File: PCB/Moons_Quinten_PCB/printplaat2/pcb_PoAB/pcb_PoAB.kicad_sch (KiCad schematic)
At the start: 34 parts, among them U9 ARDUINO_MKR_WAN_1310

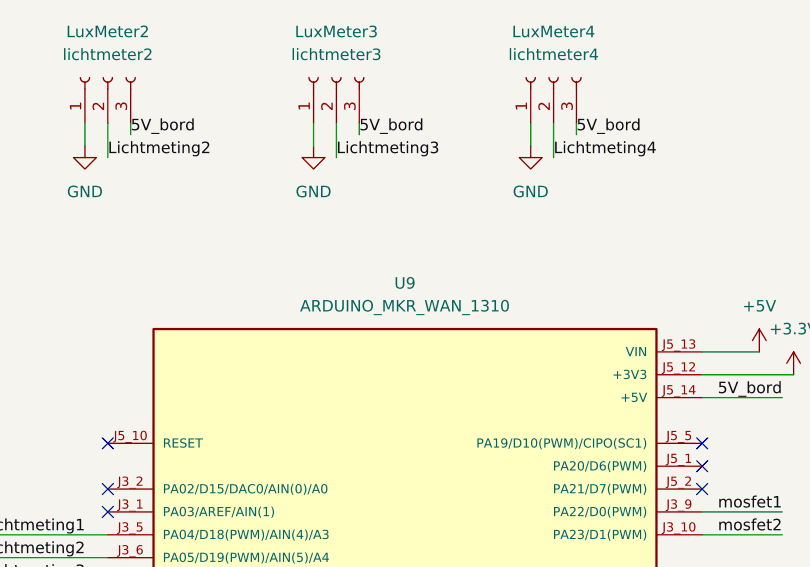
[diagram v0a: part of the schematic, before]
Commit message: pcb baseplate en docs aangepast
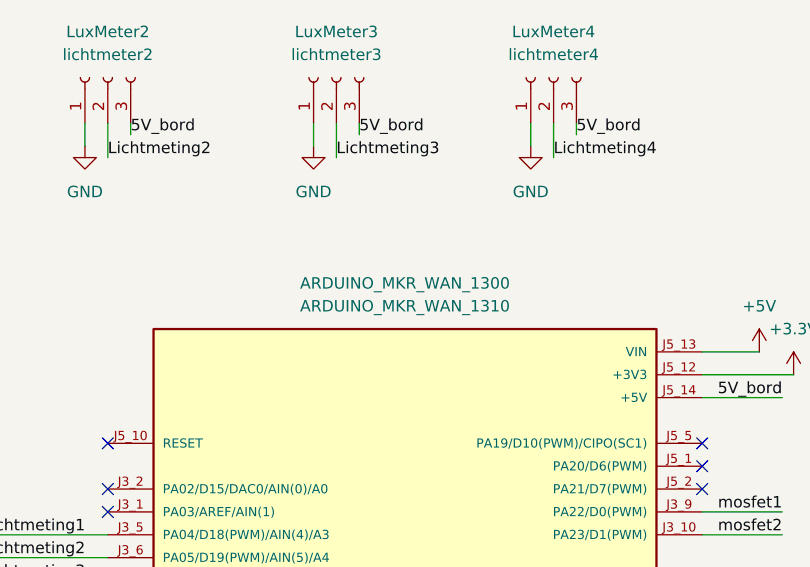
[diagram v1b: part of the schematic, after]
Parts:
- renumbered U9 to ARDUINO_MKR_WAN_1300
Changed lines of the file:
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@@
   (symbol (lib_id "ARDUINO_MKR_WAN_1310:ARDUINO_MKR_WAN_1310") (at 231.14 74.93 0) (unit 1)
     (in_bom yes) (on_board yes) (fields_autoplaced)
-    (property "Reference" "U9" (id 0) (at 231.14 44.45 0))
+    (property "Reference" "ARDUINO_MKR_WAN_1300" (id 0) (at 231.14 44.45 0))
     (property "Value" "ARDUINO_MKR_WAN_1310" (id 1) (at 231.14 46.99 0))
     (property "Footprint" "ARDUINO_MKR_WAN_1310:BOARD_ARDUINO_MKR_WAN_1310" (id 2) (at 231.14 74.93 0)
@@
       (reference "ADC_I²C1") (unit 1) (value "ADS1115") (footprint "ADS1115:MSOP10")
     )
+    (path "/c857b0ec-fa5f-4b64-98cc-3624cac25b8c"
+      (reference "ARDUINO_MKR_WAN_1300") (unit 1) (value "ARDUINO_MKR_WAN_1310") (footprint "ARDUINO_MKR_WAN_1310:BOARD_ARDUINO_MKR_WAN_1310")
+    )
     (path "/4f526e84-3b7e-432f-9b85-8c011eb508cf"
       (reference "A_meter1") (unit 1) (value "ACS712ELCTR-05B-T") (footprint "ACS712ELCTR-05B-T:SOIC127P600X175-8N")
@@
       (reference "R7") (unit 1) (value "R") (footprint "Resistor_SMD:R_0805_2012Metric_Pad1.20x1.40mm_HandSolder")
     )
-    (path "/c857b0ec-fa5f-4b64-98cc-3624cac25b8c"
-      (reference "U9") (unit 1) (value "ARDUINO_MKR_WAN_1310") (footprint "ARDUINO_MKR_WAN_1310:BOARD_ARDUINO_MKR_WAN_1310")
-    )
     (path "/82c60e96-b1be-4c38-a7f4-5b5f329b043c"
